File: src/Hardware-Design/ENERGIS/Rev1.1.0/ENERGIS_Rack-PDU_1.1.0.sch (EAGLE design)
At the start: 442 parts, among them IC1 DNI, IC10 HLW8032, IC11 HLW8032, IC12 HLW8032, IC13 MP150GJ, IC14 HLW8032, IC15 RP2040, IC16 HLW8032, IC17 MCP6001RT-I/OT, IC18 W25Q128JVPIQ, IC19 CAT24C256HU4IGT3, IC2 MP2315GJ-Z, IC20 W5500, IC21 MIC5504-3.3YM5, IC22 MCP6001RT-I/OT, IC23 MCP9700AT-E/LT, IC3 ULN2803AFWG, IC4 MCP23017T-E/ML, IC5 MP150GJ, IC6 HLW8032, IC7 HLW8032, IC8 HLW8032, IC9 SN74HC151PWR, J10 0R 1%, J2 DNI, J7 DNI, J8 0R 1%, J9 0R 1%, K1 G2RL-1A-E DC12, K2 G2RL-1A-E DC12, K3 G2RL-1A-E DC12, K4 G2RL-1A-E DC12, K5 G2RL-1A-E DC12, K6 G2RL-1A-E DC12, K7 G2RL-1A-E DC12, K8 G2RL-1A-E DC12, P12ON Green, P3ON Green, P5ON DNI, SW3 DNI, T1 BSS138, X1 12MHz, X2 25MHz

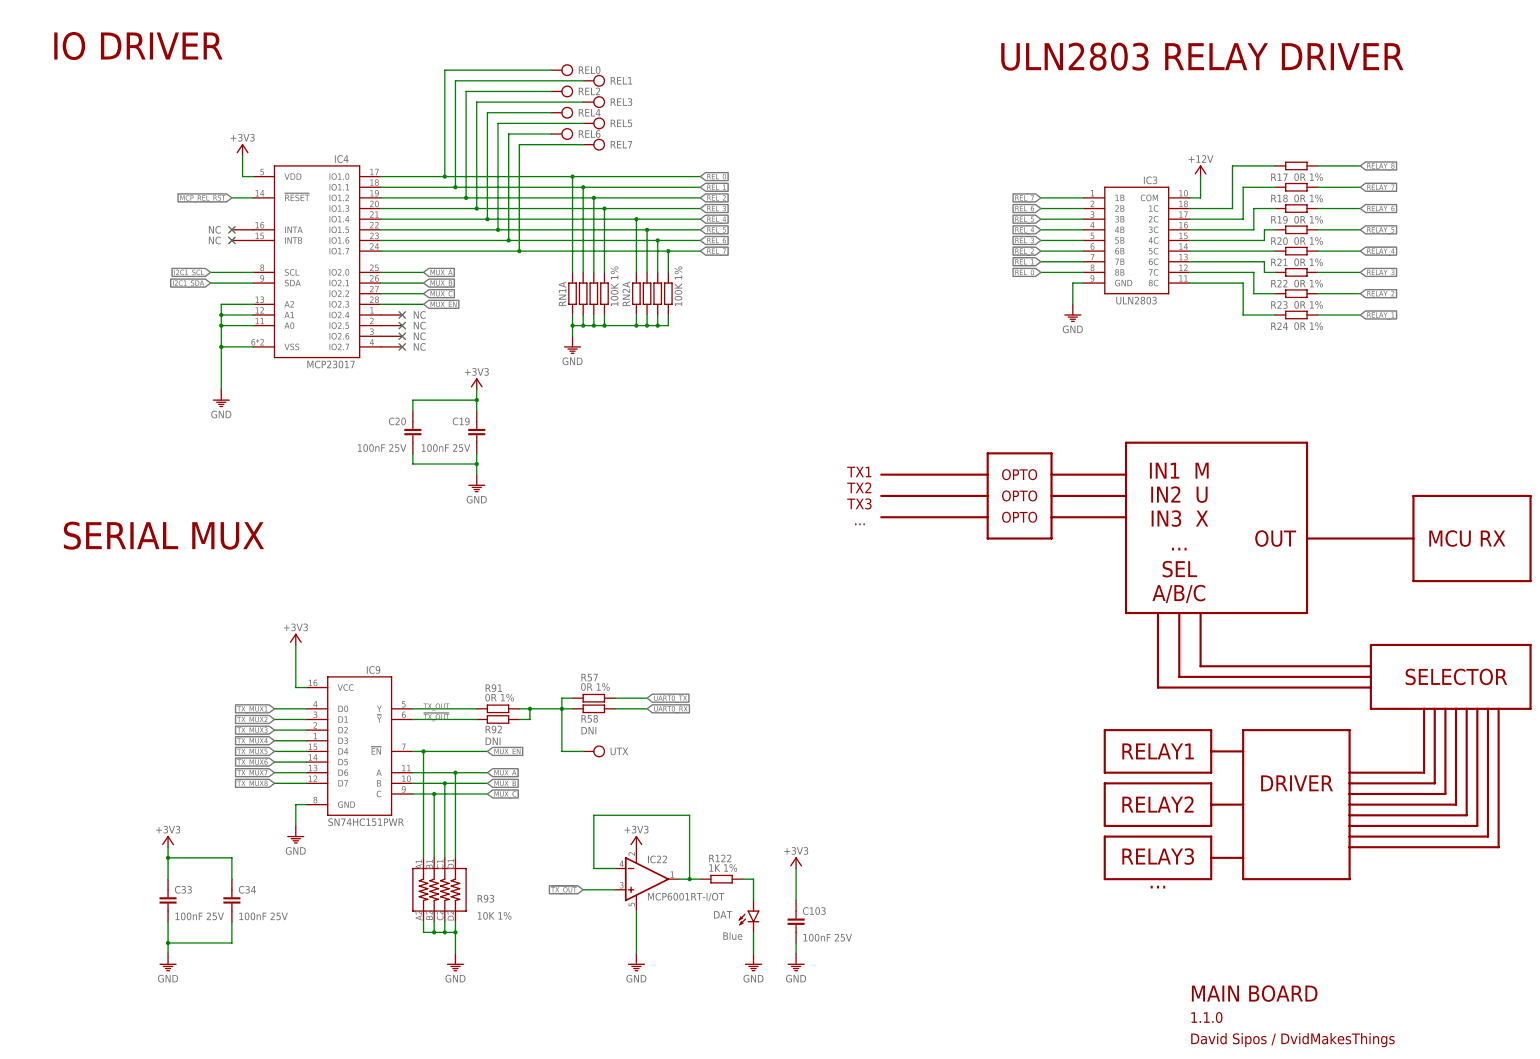
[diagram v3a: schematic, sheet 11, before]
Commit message: clear documentation, software bugfix
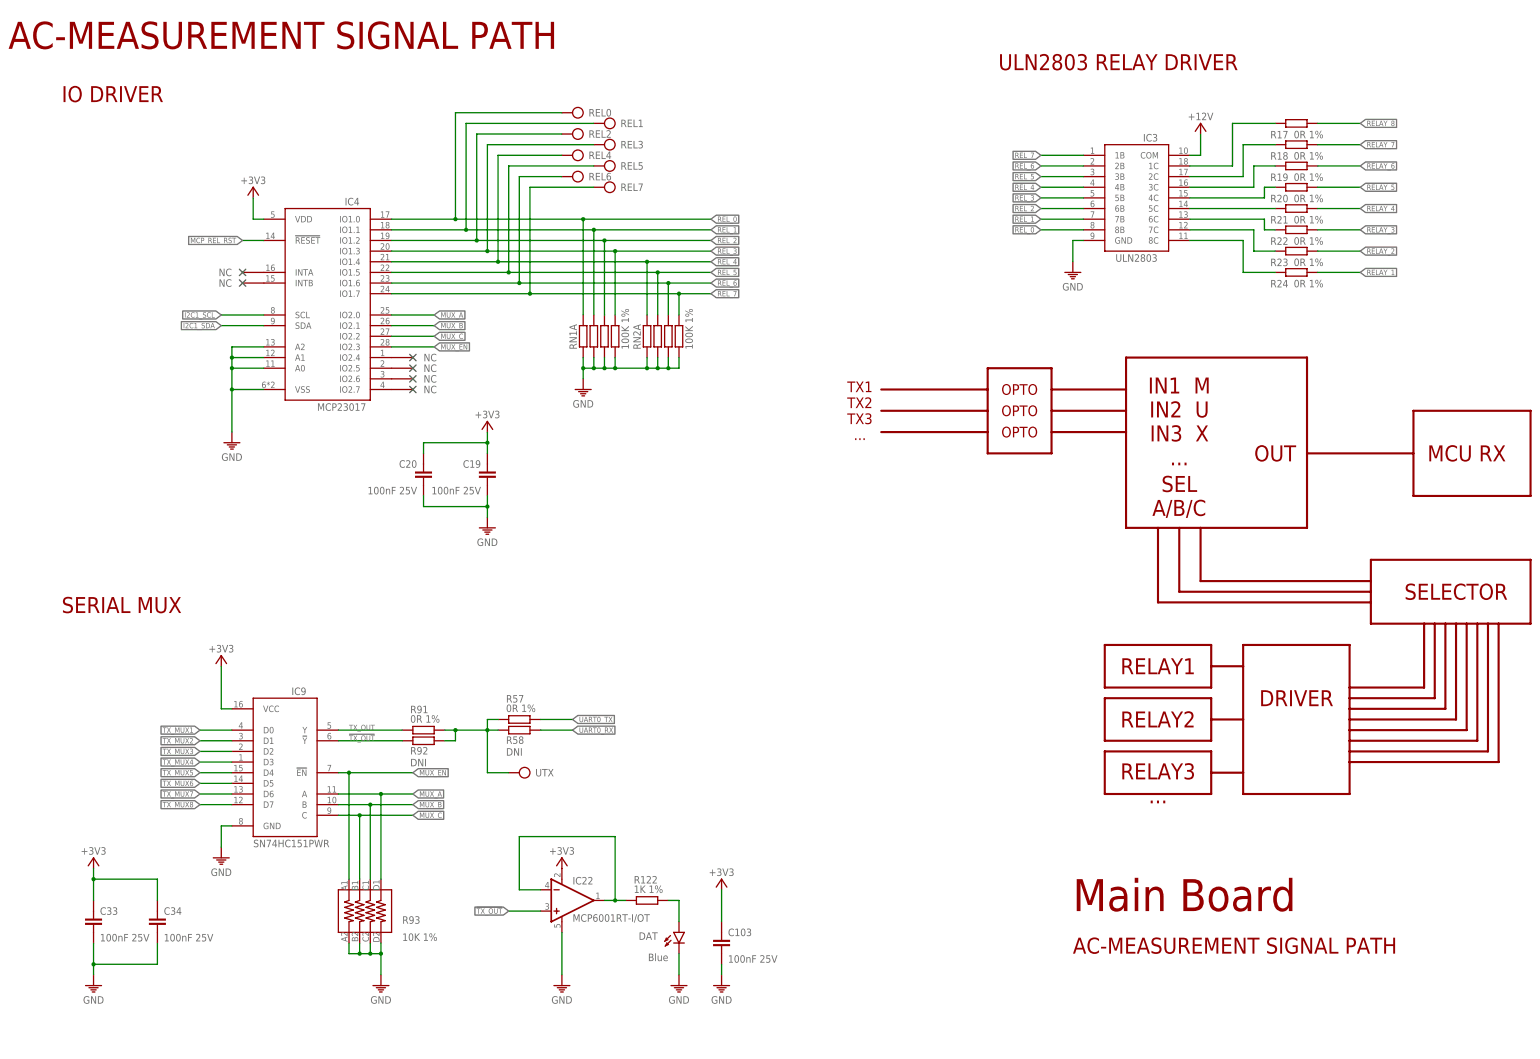
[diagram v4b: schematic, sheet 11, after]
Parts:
- REF1: device ds_ic_vreg:LM4040BXX -> ds_ic_vreg:LM4040C30FTA
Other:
- note added: "5V 200MA NON-ISOLATED POWER SUPPLY"
- note added: "AC CHANNEL MEASUREMENT I."
- note added: "AC CHANNEL MEASUREMENT II."
- note added: "AC-MEASUREMENT SIGNAL PATH"
- note added: "AC-POWER"
- note added: "CONNECTORS"
- note added: "Main Board"
- note added: "NOTE: v1.1.0 Change 5V Supply is no longer needed. That's why this MP2315 is not mounted"
- note added: "NOTE: v1.1.0 Change No separate 3.3V_MCU supply anymore. MIC is not mounted. Solder jumper is used to connect MCU supply to the main 3.3V DC/DC converter"
- note added: "NOTE: v1.1.0 Change TX_MUX5:8 was switched in 1.0.0. Due to software correction, it had no impact. Correct wiring order is now implemented from 1.1.0"
- note added: "NOTE: v1.1.0 Change USB 5V is now spearated by solder jumper. Powering the board with pure 5V only introduced software bugs, since 12V powered parts don't have their supply"
- note added: "POWER"
- note added: "RP2040 MICROCONTROLLER"
- note removed: "5V NON-ISOLATED"
- note removed: "5V, 200mA non-isolated power supply"
- note removed: "AC CHANNEL MEASUREMENT"
- note removed: "David Sipos / DvidMakesThings"
- note removed: "MAIN BOARD"
- note removed: "RP2040 MCU"
- moved on the sheet: 12VDC, 3VDC, 3VFB, 5V-NI1, 5V-NI2, 5VDC, 5VFB, AC/DC1, AC/DC2, AC_L, AC_N, ADC12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
